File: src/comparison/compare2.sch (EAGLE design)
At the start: 7 parts, among them Q1 BSS92, Q2 BSS92, Q3 BSS97, Q4 BSS97

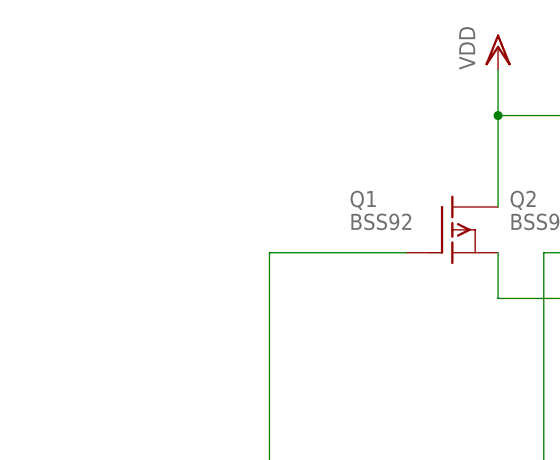
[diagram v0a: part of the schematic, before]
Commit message: added a simple test class for emf compare
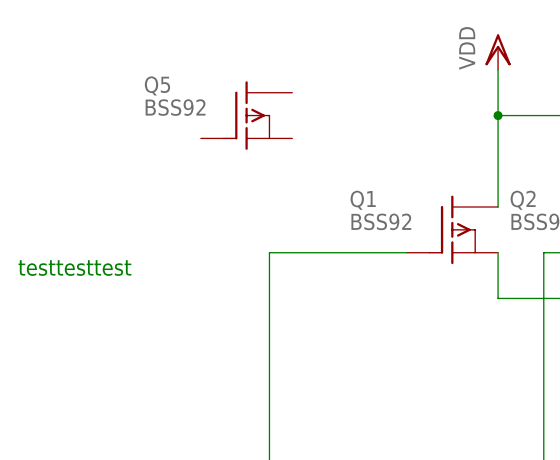
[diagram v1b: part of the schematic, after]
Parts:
- added Q5: BSS92, transistor-fet:BSS92
- Q1: TEST2 (none) -> 5; UID (none) -> 8
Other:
- note added: "testtesttest"
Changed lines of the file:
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@@
 <part name="Q1" library="transistor-fet" deviceset="BSS92" device="">
 <attribute name="P1" value="0001"/>
+<attribute name="TEST2" value="5"/>
+<attribute name="UID" value="8"/>
 </part>
 <part name="Q2" library="transistor-fet" deviceset="BSS92" device="">
@@
 <part name="A" library="pinhead" deviceset="PINHD-1X1" device=""/>
 <part name="B" library="pinhead" deviceset="PINHD-1X1" device=""/>
+<part name="Q5" library="transistor-fet" deviceset="BSS92" device="">
+<attribute name="UID" value="8"/>
+</part>
 </parts>
 <sheets>
 <sheet>
 <plain>
+<text x="-231.14" y="167.64" size="1.778" layer="91">testtesttest</text>
 </plain>
 <instances>
 <instance part="Q1" gate="G$1" x="-182.88" y="172.72">
 <attribute name="P1" x="-182.88" y="172.72" size="1.778" layer="96" display="off"/>
+<attribute name="TEST2" x="-182.88" y="172.72" size="1.778" layer="96" display="off"/>
+<attribute name="UID" x="-182.88" y="172.72" size="1.778" layer="96" display="off"/>
 </instance>
 <instance part="Q2" gate="G$1" x="-165.1" y="172.72">
@@
 <instance part="A" gate="G$1" x="-215.9" y="137.16" rot="R180"/>
 <instance part="B" gate="G$1" x="-215.9" y="119.38" rot="R180"/>
+<instance part="Q5" gate="G$1" x="-205.74" y="185.42">
+<attribute name="UID" x="-205.74" y="185.42" size="1.778" layer="96" display="off"/>
+</instance>
 </instances>
 <busses>
